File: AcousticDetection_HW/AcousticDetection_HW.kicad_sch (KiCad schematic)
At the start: 14 parts, among them U1 LM358

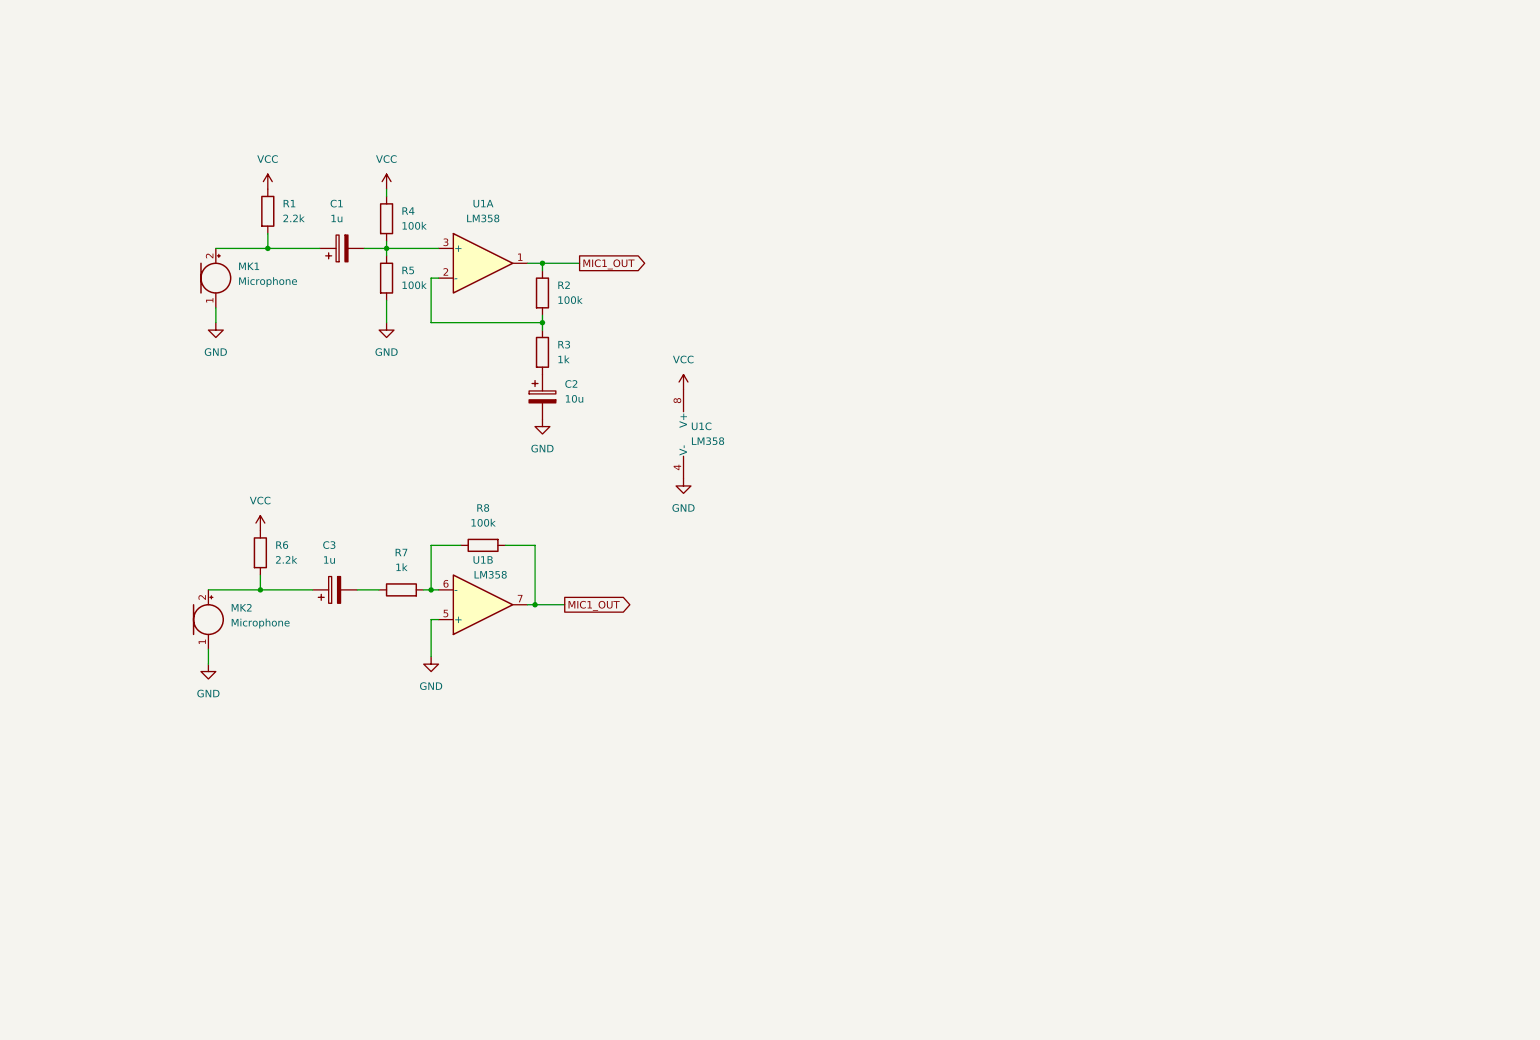
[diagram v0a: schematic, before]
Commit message: schematic update
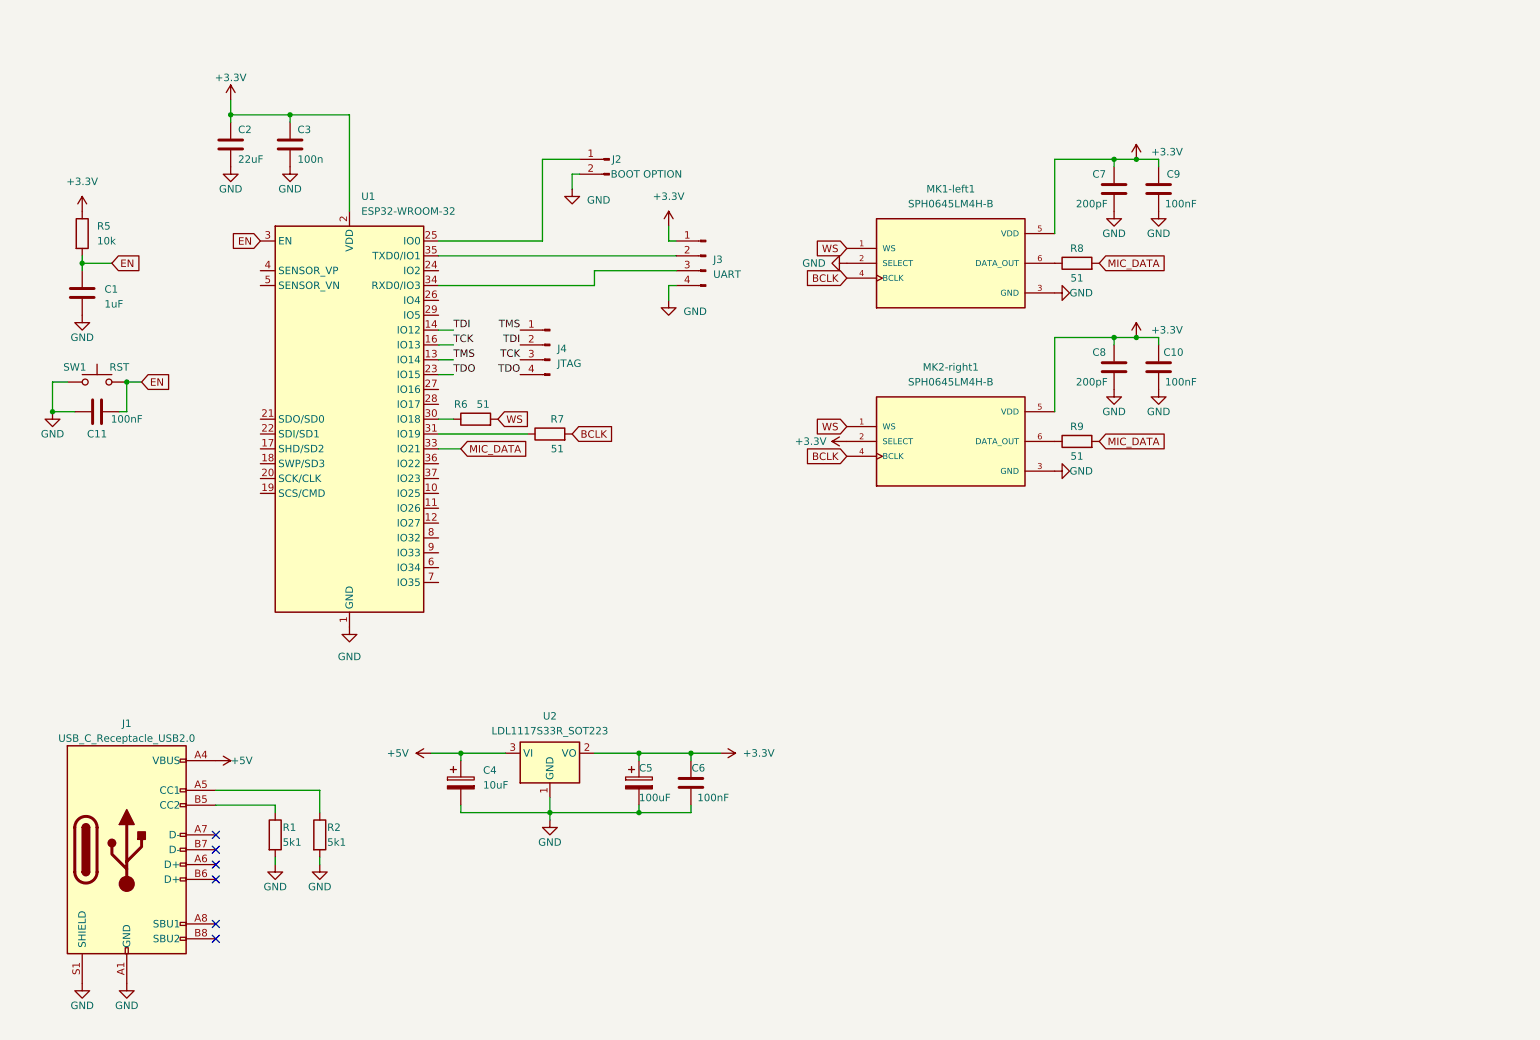
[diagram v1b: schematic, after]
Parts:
- removed C1, C3: 1u, symbol Device:C_Polarized
- removed C2: 10u, symbol Device:C_Polarized
- removed MK1, MK2: Microphone, symbol Device:Microphone
- removed R3: 1k, symbol Device:R
- removed R4: 100k, symbol Device:R
- removed U1: LM358, symbol Amplifier_Operational:LM358
- added C1: 1uF, Capacitor_SMD:C_0805_2012Metric_Pad1.18x1.45mm_HandSolder, symbol Device:C
- added C10, C9: 100nF, Capacitor_SMD:C_0603_1608Metric_Pad1.08x0.95mm_HandSolder, symbol Device:C
- added C11, C6: 100nF, Capacitor_SMD:C_0805_2012Metric_Pad1.18x1.45mm_HandSolder, symbol Device:C
- added C2: 22uF, Capacitor_SMD:C_0805_2012Metric_Pad1.18x1.45mm_HandSolder, symbol Device:C
- added C3: 100n, Capacitor_SMD:C_0805_2012Metric_Pad1.18x1.45mm_HandSolder, symbol Device:C
- added C4: 10uF, Capacitor_SMD:CP_Elec_5x3, symbol Device:C_Polarized
- added C5: 100uF, Capacitor_SMD:CP_Elec_6.3x7.7, symbol Device:C_Polarized
- added C7, C8: 200pF, Capacitor_SMD:C_0603_1608Metric_Pad1.08x0.95mm_HandSolder, symbol Device:C
- added J1: USB_C_Receptacle_USB2.0, Connector_USB:USB_C_Receptacle_GCT_USB4105-xx-A_16P_TopMnt_Horizontal, symbol Connector:USB_C_Receptacle_USB2.0
- added J2: BOOT OPTION, symbol Connector:Conn_01x02_Pin
- added J3: UART, symbol Connector:Conn_01x04_Pin
- added J4: JTAG, symbol Connector:Conn_01x04_Pin
- added MK1-left1, MK2-right1: SPH0645LM4H-B, SPH0645LM4H-B:MIC_SPH0645LM4H-B, symbol SPH0645LM4H-B:SPH0645LM4H-B
- added R9: 51, Resistor_SMD:R_0603_1608Metric_Pad0.98x0.95mm_HandSolder, symbol Device:R
- added SW1: RST, Button_Switch_SMD:SW_Tactile_SPST_NO_Straight_CK_PTS636Sx25SMTRLFS, symbol Switch:SW_Push
- added U1: ESP32-WROOM-32, RF_Module:ESP32-WROOM-32, symbol RF_Module:ESP32-WROOM-32
- added U2: LDL1117S33R_SOT223, Package_TO_SOT_SMD:SOT-223-3_TabPin2, symbol Regulator_Linear:LD1117S33TR_SOT223
- R1: value 2.2k -> 5k1
- R2: value 100k -> 5k1
- R5: value 100k -> 10k; footprint (none) -> Resistor_SMD:R_0805_2012Metric_Pad1.20x1.40mm_HandSolder
- R6: value 2.2k -> 51; footprint (none) -> Resistor_SMD:R_0603_1608Metric_Pad0.98x0.95mm_HandSolder
- R7: value 1k -> 51; footprint (none) -> Resistor_SMD:R_0603_1608Metric_Pad0.98x0.95mm_HandSolder
- R8: value 100k -> 51; footprint (none) -> Resistor_SMD:R_0603_1608Metric_Pad0.98x0.95mm_HandSolder
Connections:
- net GND: now also R1.2, R2.2, C1.1, C10.1, C11.1, C2.1, C3.1, C4.2, C5.2, C6.2, C7.1, C8.1, C9.1, J1.A1 (GND), J1.A12 (GND), J1.B1 (GND), J1.B12 (GND), J1.S1 (SHIELD), J2.2 (Pin_2), J3.4 (Pin_4), MK1-left1.2 (SELECT), MK1-left1.3 (GND), MK2-right1.3 (GND), SW1.1, U1.1 (GND), U1.15 (GND), U1.38 (GND), U1.39 (GND), U2.1 (GND); no longer R5.2
- net at R8.1: now also MK1-left1.6 (DATA_OUT); no longer R7.2
- net at R7.1: now also U1.31 (IO19)
- net +3.3V: now reaches R5.1
- net +3.3V: now also C10.2, C2.2, C3.2, C5.1, C6.1, C7.2, C8.2, C9.2, J3.1 (Pin_1), MK1-left1.5 (VDD), MK2-right1.2 (SELECT), MK2-right1.5 (VDD), U1.2 (VDD), U2.2 (VO)
- net WS: now reaches R6.2
- net WS: now also MK1-left1.1 (WS), MK2-right1.1 (WS)
- net MIC1_OUT: no longer names the net of R2.1
- net MIC1_OUT: now also J1.A5 (CC1); no longer R8.2
- net VCC: no longer names the net of R1.1
- net VCC: now also J1.B5 (CC2); no longer R6.1
- new net: MK2-right1.6 (DATA_OUT), R9.1
- new net: J2.1 (Pin_1), U1.25 (IO0)
- new net: R6.1, U1.30 (IO18)
- new net: J3.2 (Pin_2), U1.35 (TXD0/IO1)
- new net: J3.3 (Pin_3), U1.34 (RXD0/IO3)
- new net +5V: C4.1, J1.A4 (VBUS), J1.A9 (VBUS), J1.B4 (VBUS), J1.B9 (VBUS), U2.3 (VI)
- new net BCLK: MK1-left1.4 (BCLK), MK2-right1.4 (BCLK), R7.2
- new net EN: C1.2, C11.2, R5.2, SW1.2, U1.3 (EN)
- new net MIC_DATA: R8.2, R9.2, U1.33 (IO21)
- new net TCK: J4.3 (Pin_3), U1.16 (IO13)
- new net TDI: J4.2 (Pin_2), U1.14 (IO12)
- new net TDO: J4.4 (Pin_4), U1.23 (IO15)
- new net TMS: J4.1 (Pin_1), U1.13 (IO14)
- no-connect marks 0 -> 6
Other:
- company: (none) -> CTU FEL, Department of Measurement
- title: (none) -> Acoustic Detection

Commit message: small fixes
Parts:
- removed C4: 10uF, Capacitor_SMD:CP_Elec_5x3, symbol Device:C_Polarized
- removed C5: 100uF, Capacitor_SMD:CP_Elec_6.3x7.7, symbol Device:C_Polarized
- removed C6: 100nF, Capacitor_SMD:C_0805_2012Metric_Pad1.18x1.45mm_HandSolder, symbol Device:C
- added C4, C5: 10uF, Capacitor_SMD:C_1206_3216Metric_Pad1.33x1.80mm_HandSolder, symbol Device:C
- added D1: POWER LED, LED_SMD:LED_0805_2012Metric_Pad1.15x1.40mm_HandSolder, symbol Device:LED
- added D2: INFO LED, LED_SMD:LED_0805_2012Metric_Pad1.15x1.40mm_HandSolder, symbol Device:LED
- added J10, J9: PWR_R, AcousticDetection_extras:PowerConnector, symbol AcousticDetection_extras:PowerConnector
- added J11, J12: DATA_R, AcousticDetection_extras:DataConnector, symbol AcousticDetection_extras:DataConnector
- added J5, J6: PWR_L, AcousticDetection_extras:PowerConnector, symbol AcousticDetection_extras:PowerConnector
- added J7, J8: DATA_L, AcousticDetection_extras:DataConnector, symbol AcousticDetection_extras:DataConnector
- added R3, R4: R, Capacitor_SMD:C_0805_2012Metric_Pad1.18x1.45mm_HandSolder, symbol Device:R
- added SW2: BOOT, Button_Switch_SMD:SW_Tactile_SPST_NO_Straight_CK_PTS636Sx25SMTRLFS, symbol Switch:SW_Push
- C10, C7, C8, C9: footprint Capacitor_SMD:C_0603_1608Metric_Pad1.08x0.95mm_HandSolder -> Capacitor_SMD:C_0805_2012Metric_Pad1.18x1.45mm_HandSolder
- C2: footprint Capacitor_SMD:C_0805_2012Metric_Pad1.18x1.45mm_HandSolder -> Capacitor_SMD:C_1206_3216Metric_Pad1.33x1.80mm_HandSolder
- J2: footprint (none) -> Connector_PinHeader_2.54mm:PinHeader_1x02_P2.54mm_Vertical
- J3, J4: footprint (none) -> Connector_PinHeader_2.54mm:PinHeader_1x04_P2.54mm_Vertical
- R1, R2: footprint (none) -> Capacitor_SMD:C_0805_2012Metric_Pad1.18x1.45mm_HandSolder
- R6, R7, R8, R9: footprint Resistor_SMD:R_0603_1608Metric_Pad0.98x0.95mm_HandSolder -> Resistor_SMD:R_0805_2012Metric_Pad1.20x1.40mm_HandSolder
- SW1: value RST -> EN
- renumbered C11 to C6
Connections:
- net +3.3V: now also J3.4 (Pin_4), C5.1, J5.1 (3V3), J9.1 (3V3), R3.2; no longer C10.2, C7.2, C8.2, C9.2, J3.1 (Pin_1), MK1-left1.5 (VDD), MK2-right1.2 (SELECT), MK2-right1.5 (VDD)
- net +5V: now also C4.1
- net BCLK: now also J11.1 (BCLK), J7.1 (BCLK); no longer MK1-left1.4 (BCLK), MK2-right1.4 (BCLK)
- net GND: now also J3.1 (Pin_1), C4.2, C5.2, D1.1 (K), D2.1 (K), J5.2 (GND), J9.2 (GND), SW2.2; no longer C10.1, C7.1, C8.1, C9.1, J2.2 (Pin_2), J3.4 (Pin_4), MK1-left1.2 (SELECT), MK1-left1.3 (GND), MK2-right1.3 (GND)
- net MIC_DATA: now also J11.2 (DATA), J7.2 (DATA); no longer R8.2, R9.2
- net WS: now also J11.3 (WS), J7.3 (WS); no longer MK1-left1.1 (WS), MK2-right1.1 (WS)
- net at U1.25 (IO0): now also SW2.1; no longer J2.1 (Pin_1)
- net RXD: now reaches J3.2 (Pin_2)
- net RXD: now also U1.34 (RXD0/IO3); no longer U1.35 (TXD0/IO1)
- net TXD: now reaches J3.3 (Pin_3)
- net TXD: now also U1.35 (TXD0/IO1); no longer U1.34 (RXD0/IO3)
- net INFO_LED: now reaches U1.24 (IO2)
- net INFO_LED: now also R4.2
- new net: C7.2, C9.2, J6.1 (3V3), MK1-left1.5 (VDD)
- new net: D1.2 (A), R3.1
- new net: D2.2 (A), R4.1
- new net 3V3_R: C10.2, C8.2, J10.1 (3V3), MK2-right1.2 (SELECT), MK2-right1.5 (VDD)
- new net BCLK_L: J8.1 (BCLK), MK1-left1.4 (BCLK)
- new net BCLK_R: J12.1 (BCLK), MK2-right1.4 (BCLK)
- new net GND_L: C7.1, C9.1, J6.2 (GND), MK1-left1.2 (SELECT), MK1-left1.3 (GND)
- new net GND_R: C10.1, C8.1, J10.2 (GND), MK2-right1.3 (GND)
- new net MIC_DATA_L: J8.2 (DATA), R8.2
- new net MIC_DATA_R: J12.2 (DATA), R9.2
- new net WS_L: J8.3 (WS), MK1-left1.1 (WS)
- new net WS_R: J12.3 (WS), MK2-right1.1 (WS)
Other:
- note added: "RESET"
- moved on the sheet: C10, C7, C8, C9, J2, J3, MK1-left1, MK2-right1, R8, R9

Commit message: add POWER symbol for ERC & add parts links
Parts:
- removed J2: BOOT OPTION, Connector_PinHeader_2.54mm:PinHeader_1x02_P2.54mm_Vertical, symbol Connector:Conn_01x02_Pin
- C1: PRICE (none) -> 1.97; Shop (none) -> https://www.tme.eu/cz/details/cl21a105kbclnnc/kondenzatory-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
- C10, C9: footprint Capacitor_SMD:C_0805_2012Metric_Pad1.18x1.45mm_HandSolder -> Capacitor_SMD:C_0603_1608Metric_Pad1.08x0.95mm_HandSolder; PRICE (none) -> 0.266; Shop (none) -> https://www.tme.eu/cz/details/cc0603krx7r8104/kondenzatory-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
- C2: PRICE (none) -> 5.029; Shop (none) -> https://www.tme.eu/cz/details/grm31cr70j226ke19l/kondenzato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
- C3: value 100n -> 100nF; PRICE (none) -> 0.3056; Shop (none) -> https://www.tme.eu/cz/details/cc0805kpx7r9104/kondenzatory-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
- C4, C5: PRICE (none) -> 3.43; Shop (none) -> https://www.tme.eu/cz/details/cl31b106kqhnnne/kondenzatory-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
- C6: PRICE (none) -> 0.3056; Shop (none) -> https://www.tme.eu/cz/details/cc0805kpx7r9104/kondenzatory-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
- C7, C8: footprint Capacitor_SMD:C_0805_2012Metric_Pad1.18x1.45mm_HandSolder -> Capacitor_SMD:C_0603_1608Metric_Pad1.08x0.95mm_HandSolder; PRICE (none) -> 0.348; Shop (none) -> https://www.tme.eu/cz/details/cc0603jrnpo9bn181/kondenzator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
- D1: value POWER LED -> POWER; footprint LED_SMD:LED_0805_2012Metric_Pad1.15x1.40mm_HandSolder -> LED_SMD:LED_1206_3216Metric_Pad1.42x1.75mm_HandSolder; PRICE (none) -> 1.38; Shop (none) -> https://www.tme.eu/cz/details/ll-s150vc-v1-1b/diody-led-smd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
- D2: value INFO LED -> INFO; footprint LED_SMD:LED_0805_2012Metric_Pad1.15x1.40mm_HandSolder -> LED_SMD:LED_1206_3216Metric_Pad1.42x1.75mm_HandSolder; PRICE (none) -> 1.86; Shop (none) -> https://www.tme.eu/cz/details/ll-s150bc-b4-1a/diody-led-smd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
- J1: PRICE (none) -> 16.5; Shop (none) -> https://www.tme.eu/cz/details/usb4105-gf-a/konektory-usb-a-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
- J10, J11, J12, J3, J4, J5, J6, J7, J8, J9: PRICE (none) -> -; Shop (none) -> -
- MK1-left1, MK2-right1: PRICE None -> 72
- R1, R2: PRICE (none) -> 0.34; Shop (none) -> https://www.tme.eu/cz/details/smd0805-5k1/rezistory-smd/roy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
- R3, R4: value R -> 1k; PRICE (none) -> 2.28; Shop (none) -> https://www.tme.eu/cz/details/erjhp6f1001v/rezistory-smd/pa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
- R5: PRICE (none) -> 2.25; Shop (none) -> https://www.tme.eu/cz/details/era6aeb103v/rezistory-smd/pan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
- R6, R7: PRICE (none) -> 1.97; Shop (none) -> https://www.tme.eu/cz/details/swr0805-51r-5%25/rezistory-sm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
- R8, R9: footprint Resistor_SMD:R_0805_2012Metric_Pad1.20x1.40mm_HandSolder -> Resistor_SMD:R_0603_1608Metric_Pad0.98x0.95mm_HandSolder; PRICE (none) -> 2.08; Shop (none) -> https://www.tme.eu/cz/details/era3aeb510v/rezistory-smd/pan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
- SW1, SW2: PRICE (none) -> 7
- U1: PRICE (none) -> 75
- U2: PRICE (none) -> 5.26
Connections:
- net 3V3_L: now reaches C7.2, C9.2, J6.1 (3V3), MK1-left1.5 (VDD)
- no-connect marks 6 -> 27

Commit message: finishing pcb
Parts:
- R1, R2, R3, R4: footprint Capacitor_SMD:C_0805_2012Metric_Pad1.18x1.45mm_HandSolder -> Resistor_SMD:R_0805_2012Metric_Pad1.20x1.40mm_HandSolder
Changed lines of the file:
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@@
       (effects (font (size 1.27 1.27)) (justify left))
     )
-    (property "Footprint" "Capacitor_SMD:C_0805_2012Metric_Pad1.18x1.45mm_HandSolder" (at 68.072 153.67 90)
+    (property "Footprint" "Resistor_SMD:R_0805_2012Metric_Pad1.20x1.40mm_HandSolder" (at 68.072 153.67 90)
       (effects (font (size 1.27 1.27)) hide)
     )
@@
       (effects (font (size 1.27 1.27)) (justify left))
     )
-    (property "Footprint" "Capacitor_SMD:C_0805_2012Metric_Pad1.18x1.45mm_HandSolder" (at 75.692 153.67 90)
+    (property "Footprint" "Resistor_SMD:R_0805_2012Metric_Pad1.20x1.40mm_HandSolder" (at 75.692 153.67 90)
       (effects (font (size 1.27 1.27)) hide)
     )
@@
       (effects (font (size 1.27 1.27)) (justify right))
     )
-    (property "Footprint" "Capacitor_SMD:C_0805_2012Metric_Pad1.18x1.45mm_HandSolder" (at 178.308 144.145 90)
+    (property "Footprint" "Resistor_SMD:R_0805_2012Metric_Pad1.20x1.40mm_HandSolder" (at 178.308 144.145 90)
       (effects (font (size 1.27 1.27)) hide)
     )
@@
       (effects (font (size 1.27 1.27)) (justify right))
     )
-    (property "Footprint" "Capacitor_SMD:C_0805_2012Metric_Pad1.18x1.45mm_HandSolder" (at 197.358 144.145 90)
-      (effects (font (size 1.27 1.27)) hide)
-    )
+    (property "Footprint" "Resistor_SMD:R_0805_2012Metric_Pad1.20x1.40mm_HandSolder" (at 197.358 144.145 90)
+      (effects (font (size 1.27 1.27)) hide)
+    )

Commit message: the resistor values of pcb leds were changed to 220R
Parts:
- R3, R4: value 1k -> 220R
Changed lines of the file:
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@@
   )
   (symbol (lib_id "Device:R") (at 176.53 144.145 180) (unit 1)
-    (in_bom yes) (on_board yes) (dnp no) (fields_autoplaced)
+    (in_bom yes) (on_board yes) (dnp no)
     (property "Reference" "R3" (at 179.07 143.51 0)
       (effects (font (size 1.27 1.27)) (justify right))
     )
-    (property "Value" "1k" (at 179.07 146.05 0)
+    (property "Value" "220R" (at 179.07 146.05 0)
       (effects (font (size 1.27 1.27)) (justify right))
     )
@@
       (effects (font (size 1.27 1.27)) (justify right))
     )
-    (property "Value" "1k" (at 198.12 146.05 0)
-      (effects (font (size 1.27 1.27)) (justify right))
-    )
+    (property "Value" "220R" (at 198.12 146.05 0)
+      (effects (font (size 1.27 1.27)) (justify right))
+    )

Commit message: schematic cleanup
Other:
- company: CTU FEL, Department of Measurement -> Matěj Trnka, CTU FEL, Department of Measurement
- moved on the sheet: C1, C10, C2, C3, C4, C5, C6, C7, C8, C9, D1, D2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
